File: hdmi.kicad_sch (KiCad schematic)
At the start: 34 parts, among them J5 HDMI_A, J6 Conn_01x03, SW1 SW_DIP_x03, U1 TFP410PAPR, U2 MIC5205-5.0YM5, U8 PCA9306DCU

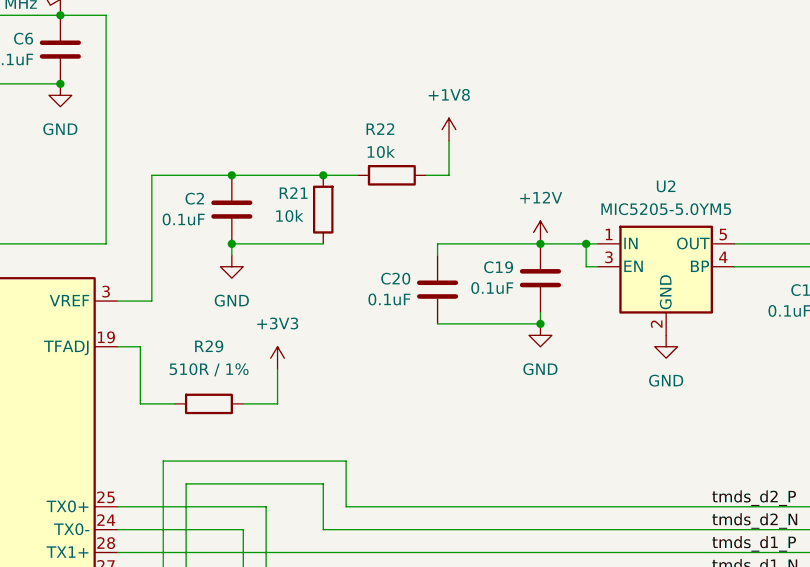
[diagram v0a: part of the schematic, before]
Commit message: Fixed wrong FMC pin labels
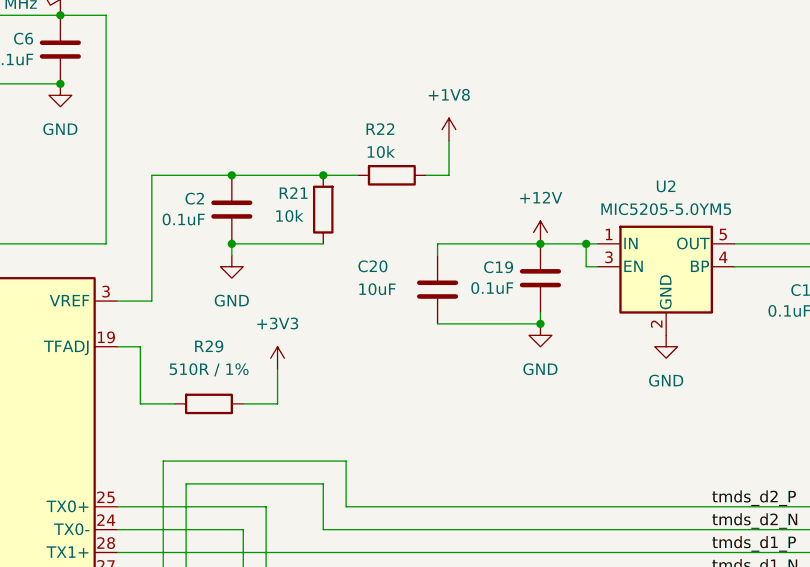
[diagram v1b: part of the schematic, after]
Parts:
- C20: value 0.1uF -> 10uF; footprint Capacitor_SMD:C_0402_1005Metric -> Capacitor_SMD:C_0603_1608Metric; Alternative MPNs C0402C104K8PAC -> (none); Link to Alternative https://www.mouser.de/ProductDetail/KEMET/C0402C104K8PAC?qs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 -> (none); MFG TAIYO YUDEN -> TAIYO YUDEN; MPN MBAST105SB7104KFNA01 -> MSAST168BB5106MTNA01; Supplier Link https://www.mouser.de/ProductDetail/TAIYO-YUDEN/MBAST105SB7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 -> https://www.mouser.de/ProductDetail/TAIYO-YUDEN/MSAST168BB5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
- R29: MFG (none) -> Yageo; MPN (none) -> RC0402DR-07510RL; Supplier Link (none) -> https://www.mouser.de/ProductDetail/YAGEO/RC0402DR-07510RL?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
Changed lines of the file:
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@@
 	)
 	(symbol
-		(lib_id "Device:C")
-		(at 199.39 57.15 0)
-		(mirror y)
-		(unit 1)
-		(exclude_from_sim no)
-		(in_bom yes)
-		(on_board yes)
-		(dnp no)
-		(property "Reference" "C20"
-			(at 196.469 55.9816 0)
-			(effects
-				(font
-					(size 1.27 1.27)
-				)
-				(justify left)
-			)
-		)
-		(property "Value" "0.1uF"
-			(at 196.469 58.293 0)
-			(effects
-				(font
-					(size 1.27 1.27)
-				)
-				(justify left)
-			)
-		)
-		(property "Footprint" "Capacitor_SMD:C_0402_1005Metric"
-			(at 198.4248 60.96 0)
-			(effects
-				(font
-					(size 1.27 1.27)
-				)
-				(hide yes)
-			)
-		)
-		(property "Datasheet" "~"
-			(at 199.39 57.15 0)
-			(effects
-				(font
-					(size 1.27 1.27)
-				)
-				(hide yes)
-			)
-		)
-		(property "Description" "Unpolarized capacitor"
-			(at 199.39 57.15 0)
-			(effects
-				(font
-					(size 1.27 1.27)
-				)
-				(hide yes)
-			)
-		)
-		(property "MPN" "MBAST105SB7104KFNA01"
-			(at 199.39 57.15 0)
-			(effects
-				(font
-					(size 1.27 1.27)
-				)
-				(hide yes)
-			)
-		)
-		(property "Supplier Link" "https://www.mouser.de/ProductDetail/TAIYO-YUDEN/MBAST105SB7104KFNA01?qs=tlsG%2FOw5FFj0FpJuqULGiw%3D%3D "
-			(at 199.39 57.15 0)
-			(effects
-				(font
-					(size 1.27 1.27)
-				)
-				(hide yes)
-			)
-		)
-		(property "Link to Alternative" "https://www.mouser.de/ProductDetail/KEMET/C0402C104K8PAC?qs=gnaPJ2cis71t%2F81aE9FjIg%3D%3D"
-			(at 199.39 57.15 0)
-			(effects
-				(font
-					(size 1.27 1.27)
-				)
-				(hide yes)
-			)
-		)
-		(property "MFG" " TAIYO YUDEN"
-			(at 199.39 57.15 0)
-			(effects
-				(font
-					(size 1.27 1.27)
-				)
-				(hide yes)
-			)
-		)
-		(property "Alternative MPNs" "C0402C104K8PAC"
-			(at 199.39 57.15 0)
-			(effects
-				(font
-					(size 1.27 1.27)
-				)
-				(hide yes)
-			)
-		)
-		(pin "1"
-		)
-		(pin "2"
-		)
-		(instances
-			(project "fmc-module"
-				(path "/d19e166d-341d-462a-80b4-f2bdffaa1825/1457e6e0-ad1e-4378-a600-a6902f50d75d"
-					(reference "C20")
-					(unit 1)
-				)
-			)
-		)
-	)
-	(symbol
 		(lib_id "power:+5V")
 		(at 261.62 49.53 0)
@@
 			)
 		)
+		(property "MFG" "Yageo"
+			(at 173.99 69.85 90)
+			(effects
+				(font
+					(size 1.27 1.27)
+				)
+				(hide yes)
+			)
+		)
+		(property "MPN" " RC0402DR-07510RL"
+			(at 173.99 69.85 90)
+			(effects
+				(font
+					(size 1.27 1.27)
+				)
+				(hide yes)
+			)
+		)
+		(property "Supplier Link" "https://www.mouser.de/ProductDetail/YAGEO/RC0402DR-07510RL?qs=sGAEpiMZZMtG0KNrPCHnjdddqoDGo00GPkFvp667YOVfGt7QWtVpuw%3D%3D"
+			(at 173.99 69.85 90)
+			(effects
+				(font
+					(size 1.27 1.27)
+				)
+				(hide yes)
+			)
+		)
 		(pin "2"
 		)
@@
 					(unit 1)
 				)
+			)
+		)
+	)
+	(symbol
+		(lib_id "Device:C")
+		(at 199.39 57.15 0)
+		(unit 1)
+		(exclude_from_sim no)
+		(in_bom yes)
+		(on_board yes)
+		(dnp no)
+		(property "Reference" "C20"
+			(at 190.5 54.61 0)
+			(effects
+				(font
+					(size 1.27 1.27)
+				)
+				(justify left)
+			)
+		)
+		(property "Value" "10uF"
+			(at 190.5 57.15 0)
+			(effects
+				(font
+					(size 1.27 1.27)
+				)
+				(justify left)
+			)
+		)
+		(property "Footprint" "Capacitor_SMD:C_0603_1608Metric"
+			(at 200.3552 60.96 0)
+			(effects
+				(font
+					(size 1.27 1.27)
+				)
+				(hide yes)
+			)
+		)
+		(property "Datasheet" "~"
+			(at 199.39 57.15 0)
+			(effects
+				(font
+					(size 1.27 1.27)
+				)
+				(hide yes)
+			)
+		)
+		(property "Description" "Unpolarized capacitor"
+			(at 199.39 57.15 0)
+			(effects
+				(font
+					(size 1.27 1.27)
+				)
+				(hide yes)
+			)
+		)
+		(property "MFG" "TAIYO YUDEN"
+			(at 199.39 57.15 0)
+			(effects
+				(font
+					(size 1.27 1.27)
+				)
+				(hide yes)
+			)
+		)
+		(property "MPN" "MSAST168BB5106MTNA01 "
+			(at 199.39 57.15 0)
+			(effects
+				(font
+					(size 1.27 1.27)
+				)
+				(hide yes)
+			)
+		)
+		(property "Supplier Link" "https://www.mouser.de/ProductDetail/TAIYO-YUDEN/MSAST168BB5106MTNA01?qs=tlsG%2FOw5FFiY5MKT99fx9A%3D%3D"
+			(at 199.39 57.15 0)
+			(effects
+				(font
+					(size 1.27 1.27)
+				)
+				(hide yes)
+			)
+		)
+		(property "Sim.Device" ""
+			(at 199.39 57.15 0)
+			(effects
+				(font
+					(size 1.27 1.27)
+				)
+				(hide yes)
+			)
+		)
+		(property "Sim.Pins" ""
+			(at 199.39 57.15 0)
+			(effects
+				(font
+					(size 1.27 1.27)
+				)
+				(hide yes)
+			)
+		)
+		(pin "1"
+		)
+		(pin "2"
+		)
+		(instances
+			(project "fmc-module"
+				(path "/d19e166d-341d-462a-80b4-f2bdffaa1825/1457e6e0-ad1e-4378-a600-a6902f50d75d"
+					(reference "C20")
+					(unit 1)
+				)
